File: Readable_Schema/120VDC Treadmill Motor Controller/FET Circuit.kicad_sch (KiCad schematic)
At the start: 5 parts, among them Q2 IRFB4227PBF, U2 FOD3182

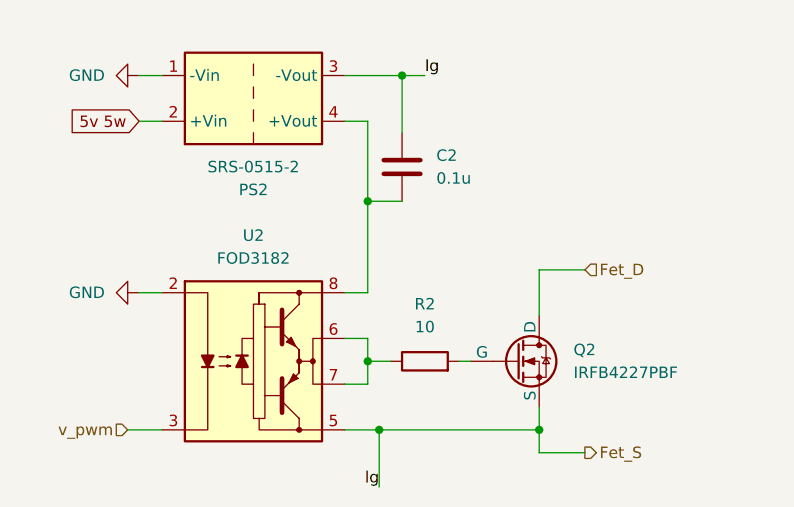
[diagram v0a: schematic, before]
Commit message: Continuing to update footprints, did some follow up math on low pass filter for adc voltage coming out of current sense system
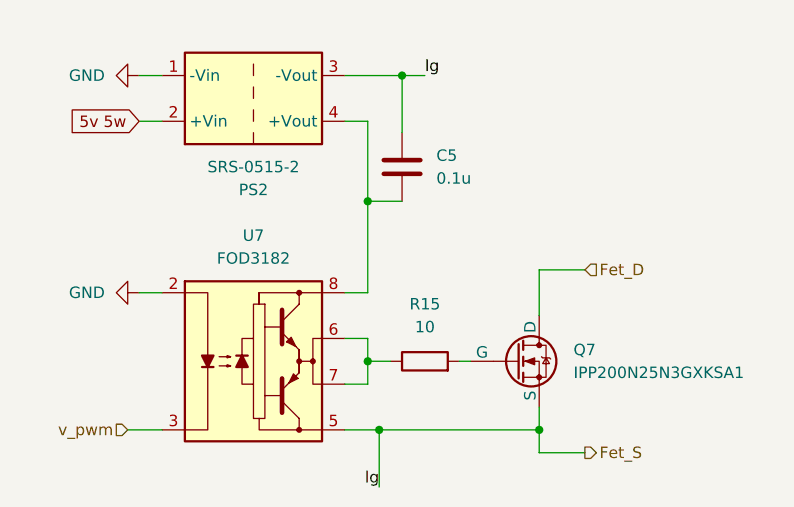
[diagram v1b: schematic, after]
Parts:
- Q7: renamed from Q2; value IRFB4227PBF -> IPP200N25N3GXKSA1
- renumbered C2 to C5, R2 to R15, U2 to U7
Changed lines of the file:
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@@
 		(dnp no)
 		(fields_autoplaced yes)
-		(property "Reference" "#PWR?"
+		(property "Reference" "#PWR0101"
 			(at 91.44 60.96 0)
 			(effects
@@
 				)
 				(path "/319bc5c0-2dd5-4df3-a34b-9170833ebccd/49a5a11b-8174-445d-b343-1fe5ec8c60de/6d3d8f4c-8a5d-4b0c-94fd-c45e8627b14b"
-					(reference "#PWR?")
+					(reference "#PWR0101")
 					(unit 1)
 				)
@@
 		(dnp no)
 		(fields_autoplaced yes)
-		(property "Reference" "#PWR?"
+		(property "Reference" "#PWR0102"
 			(at 91.44 85.09 0)
 			(effects
@@
 				)
 				(path "/319bc5c0-2dd5-4df3-a34b-9170833ebccd/49a5a11b-8174-445d-b343-1fe5ec8c60de/6d3d8f4c-8a5d-4b0c-94fd-c45e8627b14b"
-					(reference "#PWR?")
+					(reference "#PWR0102")
 					(unit 1)
 				)
@@
 		(dnp no)
 		(fields_autoplaced yes)
-		(property "Reference" "C?"
+		(property "Reference" "C5"
 			(at 130.81 69.8499 0)
 			(effects
@@
 				)
 				(path "/319bc5c0-2dd5-4df3-a34b-9170833ebccd/49a5a11b-8174-445d-b343-1fe5ec8c60de/6d3d8f4c-8a5d-4b0c-94fd-c45e8627b14b"
-					(reference "C?")
+					(reference "C5")
 					(unit 1)
 				)
@@
 		(dnp no)
 		(fields_autoplaced yes)
-		(property "Reference" "Q?"
+		(property "Reference" "Q7"
 			(at 146.05 91.4399 0)
 			(effects
@@
 			)
 		)
-		(property "Value" "IRFB4227PBF"
+		(property "Value" "IPP200N25N3GXKSA1"
 			(at 146.05 93.9799 0)
 			(effects
@@
 			)
 		)
-		(property "Datasheet" "https://www.infineon.com/assets/row/public/documents/24/49/infineon-irfb4227-datasheet-en.pdf"
+		(property "Datasheet" "https://www.infineon.com/assets/row/public/documents/24/49/infineon-ipp-b-i-200n25n3-g-datasheet-en.pdf?folderId=db3a3043163797a6011637d4bae7003b&fileId=db3a3043243b5f17012496b87e9f1971"
 			(at 139.7 105.41 0)
 			(effects
@@
 				)
 				(path "/319bc5c0-2dd5-4df3-a34b-9170833ebccd/49a5a11b-8174-445d-b343-1fe5ec8c60de/6d3d8f4c-8a5d-4b0c-94fd-c45e8627b14b"
-					(reference "Q?")
+					(reference "Q7")
 					(unit 1)
 				)
@@
 		(dnp no)
 		(fields_autoplaced yes)
-		(property "Reference" "R?"
+		(property "Reference" "R15"
 			(at 129.54 86.36 90)
 			(effects
@@
 				)
 				(path "/319bc5c0-2dd5-4df3-a34b-9170833ebccd/49a5a11b-8174-445d-b343-1fe5ec8c60de/6d3d8f4c-8a5d-4b0c-94fd-c45e8627b14b"
-					(reference "R?")
+					(reference "R15")
 					(unit 1)
 				)
@@
 		(dnp no)
 		(fields_autoplaced yes)
-		(property "Reference" "U?"
+		(property "Reference" "U7"
 			(at 110.49 78.74 0)
 			(effects
@@
 				)
 				(path "/319bc5c0-2dd5-4df3-a34b-9170833ebccd/49a5a11b-8174-445d-b343-1fe5ec8c60de/6d3d8f4c-8a5d-4b0c-94fd-c45e8627b14b"
-					(reference "U?")
-					(unit 1)
-				)
+					(reference "U7")
+					(unit 1)
+				)

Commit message: continued to add footprints, we still need to add hall effect circuit and possible brake resistor subcircuit. We may also want to consider switching the large 15v isolated power supplies to be smd as well as the FOD3182. Otherwise this will become a lot to hand solder.
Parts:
- R15: footprint (none) -> Resistor_SMD:R_0201_0603Metric_Pad0.64x0.40mm_HandSolder
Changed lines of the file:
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@@
 			)
 		)
-		(property "Footprint" ""
+		(property "Footprint" "Resistor_SMD:R_0201_0603Metric_Pad0.64x0.40mm_HandSolder"
 			(at 129.54 94.488 90)
 			(effects
@@
 			)
 		)
-		(property "Datasheet" "~"
+		(property "Datasheet" "https://industrial.panasonic.com/cdbs/www-data/pdf/RDP0000/AOA0000C337.pdf"
 			(at 129.54 92.71 0)
 			(effects
@@
 			)
 		)
-		(property "Description" "Resistor"
+		(property "Description" "ERJ-UP3J100V"
 			(at 129.54 92.71 0)
 			(effects

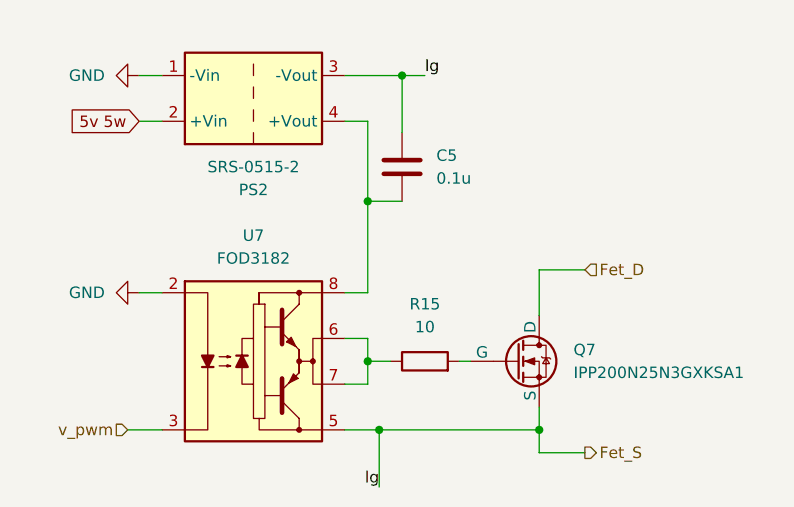
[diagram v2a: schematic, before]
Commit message: -There are no power supply/ gate driver variants for the ones chosen that support smd -We NEED to workout how we want to communicate with both linuxCNC for the CNC controller and a potentiometer for the bridgeport -We NEED to incorporate a ESTOP component that directly shuts off the motor -Missing brake resistor subcircuit -Missing Input capacitors to deal with back EMF
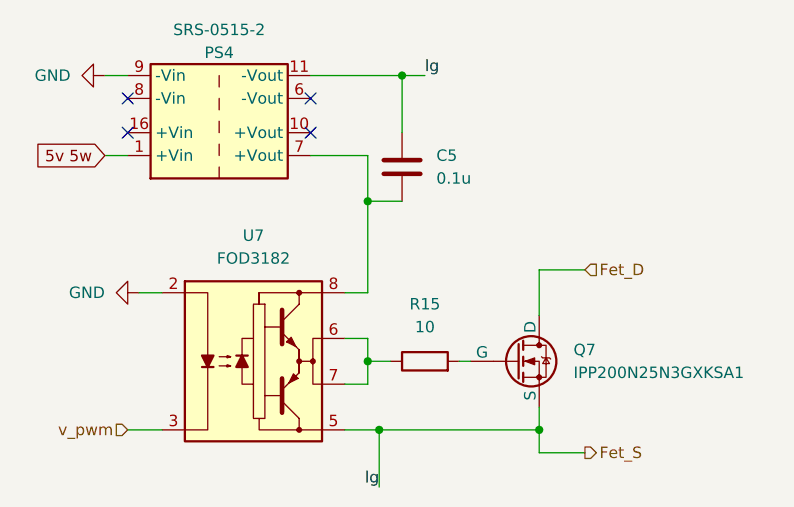
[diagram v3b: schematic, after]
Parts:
- removed PS2: SRS-0515-2, Footprints_TMC:SRS-0515 DIP-16_W7.62mm, symbol Converter_DCDC:MEE1S0303SC
- added PS4: SRS-0515-2, Footprints_TMC:SRS-0515 DIP-16_W7.62mm, symbol Treadmill_Comp:SRS-0515-2
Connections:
- net 5v 5w: now also PS4.1 (+Vin)
- net Fet_S: now also PS4.11 (-Vout)
- net GND: now also PS4.9 (-Vin)
- net at C5.2, U7.8 (VCC): now also PS4.7 (+Vout)
- no-connect marks 0 -> 4
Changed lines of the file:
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@@
 		(color 0 0 0 0)
 	)
-	(wire
-		(pts
-			(xy 97.79 60.96) (xy 100.33 60.96)
+	(no_connect
+		(at 96.52 67.31)
+	)
+	(no_connect
+		(at 116.84 63.5)
+	)
+	(no_connect
+		(at 96.52 63.5)
+	)
+	(no_connect
+		(at 116.84 67.31)
+	)
+	(wire
+		(pts
+			(xy 123.19 69.85) (xy 123.19 74.93)
 		)
 		(stroke
@@
 	(wire
 		(pts
-			(xy 120.65 60.96) (xy 127 60.96)
+			(xy 93.98 69.85) (xy 96.52 69.85)
 		)
 		(stroke
@@
 	(wire
 		(pts
-			(xy 97.79 66.04) (xy 100.33 66.04)
+			(xy 116.84 69.85) (xy 123.19 69.85)
 		)
 		(stroke
@@
 	(wire
 		(pts
+			(xy 116.84 60.96) (xy 127 60.96)
+		)
+		(stroke
+			(width 0)
+			(type default)
+		)
+	)
+	(wire
+		(pts
+			(xy 93.98 60.96) (xy 96.52 60.96)
+		)
+		(stroke
+			(width 0)
+			(type default)
+		)
+	)
+	(wire
+		(pts
 			(xy 120.65 85.09) (xy 123.19 85.09)
 		)
@@
 	(wire
 		(pts
-			(xy 120.65 66.04) (xy 123.19 66.04)
-		)
-		(stroke
-			(width 0)
-			(type default)
-		)
-	)
-	(wire
-		(pts
 			(xy 96.52 100.33) (xy 100.33 100.33)
-		)
-		(stroke
-			(width 0)
-			(type default)
-		)
-	)
-	(wire
-		(pts
-			(xy 123.19 66.04) (xy 123.19 74.93)
 		)
 		(stroke
@@
 	(global_label "5v 5w"
 		(shape input)
-		(at 97.79 66.04 180)
+		(at 93.98 69.85 180)
 		(fields_autoplaced yes)
 		(effects
@@
 		)
 		(property "Intersheetrefs" "${INTERSHEET_REFS}"
-			(at 89.1201 66.04 0)
+			(at 85.3101 69.85 0)
 			(effects
 				(font
@@
 	)
 	(symbol
-		(lib_id "power:GND")
-		(at 97.79 60.96 270)
+		(lib_id "Treadmill_Comp:SRS-0515-2")
+		(at 106.68 67.31 0)
+		(mirror x)
 		(unit 1)
 		(exclude_from_sim no)
@@
 		(on_board yes)
 		(dnp no)
-		(fields_autoplaced yes)
-		(property "Reference" "#PWR0101"
-			(at 91.44 60.96 0)
-			(effects
-				(font
-					(size 1.27 1.27)
-				)
-				(hide yes)
-			)
-		)
-		(property "Value" "GND"
-			(at 93.98 60.9599 90)
-			(effects
-				(font
-					(size 1.27 1.27)
-				)
-				(justify right)
-			)
-		)
-		(property "Footprint" ""
-			(at 97.79 60.96 0)
-			(effects
-				(font
-					(size 1.27 1.27)
-				)
-				(hide yes)
-			)
-		)
-		(property "Datasheet" ""
-			(at 97.79 60.96 0)
-			(effects
-				(font
-					(size 1.27 1.27)
-				)
-				(hide yes)
-			)
-		)
-		(property "Description" "Power symbol creates a global label with name \"GND\" , ground"
-			(at 97.79 60.96 0)
-			(effects
-				(font
-					(size 1.27 1.27)
-				)
-				(hide yes)
-			)
+		(property "Reference" "PS4"
+			(at 106.68 58.42 0)
+			(effects
+				(font
+					(size 1.27 1.27)
+				)
+			)
+		)
+		(property "Value" "SRS-0515-2"
+			(at 106.68 55.88 0)
+			(effects
+				(font
+					(size 1.27 1.27)
+				)
+			)
+		)
+		(property "Footprint" "Footprints_TMC:SRS-0515 DIP-16_W7.62mm"
+			(at 80.01 60.96 0)
+			(effects
+				(font
+					(size 1.27 1.27)
+				)
+				(justify left)
+				(hide yes)
+			)
+		)
+		(property "Datasheet" "https://www.meanwellusa.com/upload/pdf/SRS/SRS-spec.pdf"
+			(at 133.35 59.69 0)
+			(effects
+				(font
+					(size 1.27 1.27)
+				)
+				(justify left)
+				(hide yes)
+			)
+		)
+		(property "Description" "15V isolated output"
+			(at 106.68 67.31 0)
+			(effects
+				(font
+					(size 1.27 1.27)
+				)
+				(hide yes)
+			)
+		)
+		(pin "9"
 		)
 		(pin "1"
+		)
+		(pin "16"
+		)
+		(pin "8"
+		)
+		(pin "7"
+		)
+		(pin "10"
+		)
+		(pin "6"
+		)
+		(pin "11"
 		)
 		(instances
 			(project "120VDC Treadmill Motor Controller"
 				(path "/319bc5c0-2dd5-4df3-a34b-9170833ebccd/49a5a11b-8174-445d-b343-1fe5ec8c60de/0ee8c600-4f6e-4877-94f0-4a0da87ba88d"
-					(reference "#PWR05")
+					(reference "PS5")
 					(unit 1)
 				)
 				(path "/319bc5c0-2dd5-4df3-a34b-9170833ebccd/49a5a11b-8174-445d-b343-1fe5ec8c60de/6d3d8f4c-8a5d-4b0c-94fd-c45e8627b14b"
-					(reference "#PWR0101")
+					(reference "PS4")
 					(unit 1)
 				)
@@
 	)
 	(symbol
-		(lib_id "Converter_DCDC:MEE1S0303SC")
-		(at 110.49 63.5 0)
+		(lib_id "power:GND")
+		(at 93.98 60.96 270)
 		(mirror x)
 		(unit 1)
@@
 		(on_board yes)
 		(dnp no)
-		(property "Reference" "PS2"
-			(at 110.49 73.66 0)
-			(effects
-				(font
-					(size 1.27 1.27)
-				)
-			)
-		)
-		(property "Value" "SRS-0515-2"
-			(at 110.49 71.12 0)
-			(effects
-				(font
-					(size 1.27 1.27)
-				)
-			)
-		)
-		(property "Footprint" "Footprints_TMC:SRS-0515 DIP-16_W7.62mm"
-			(at 83.82 57.15 0)
-			(effects
-				(font
-					(size 1.27 1.27)
-				)
-				(justify left)
-				(hide yes)
-			)
-		)
-		(property "Datasheet" "http://diwellshop.cafe24.com/web/DATASHEET/01_subtitle/4_POWER/2_DC-DC/SRS-0515-2/SR.pdf"
-			(at 137.16 55.88 0)
-			(effects
-				(font
-					(size 1.27 1.27)
-				)
-				(justify left)
-				(hide yes)
-			)
-		)
-		(property "Description" "isolated 1W 5V to 15V DC to DC Converter"
-			(at 110.49 63.5 0)
-			(effects
-				(font
-					(size 1.27 1.27)
-				)
-				(hide yes)
-			)
-		)
-		(pin "3"
-		)
-		(pin "4"
+		(fields_autoplaced yes)
+		(property "Reference" "#PWR025"
+			(at 87.63 60.96 0)
+			(effects
+				(font
+					(size 1.27 1.27)
+				)
+				(hide yes)
+			)
+		)
+		(property "Value" "GND"
+			(at 90.17 60.9601 90)
+			(effects
+				(font
+					(size 1.27 1.27)
+				)
+				(justify right)
+			)
+		)
+		(property "Footprint" ""
+			(at 93.98 60.96 0)
+			(effects
+				(font
+					(size 1.27 1.27)
+				)
+				(hide yes)
+			)
+		)
+		(property "Datasheet" ""
+			(at 93.98 60.96 0)
+			(effects
+				(font
+					(size 1.27 1.27)
+				)
+				(hide yes)
+			)
+		)
+		(property "Description" "Power symbol creates a global label with name \"GND\" , ground"
+			(at 93.98 60.96 0)
+			(effects
+				(font
+					(size 1.27 1.27)
+				)
+				(hide yes)
+			)
 		)
 		(pin "1"
-		)
-		(pin "2"
 		)
 		(instances
 			(project "120VDC Treadmill Motor Controller"
 				(path "/319bc5c0-2dd5-4df3-a34b-9170833ebccd/49a5a11b-8174-445d-b343-1fe5ec8c60de/0ee8c600-4f6e-4877-94f0-4a0da87ba88d"
-					(reference "PS3")
+					(reference "#PWR028")
 					(unit 1)
 				)
 				(path "/319bc5c0-2dd5-4df3-a34b-9170833ebccd/49a5a11b-8174-445d-b343-1fe5ec8c60de/6d3d8f4c-8a5d-4b0c-94fd-c45e8627b14b"
-					(reference "PS2")
-					(unit 1)
-				)
+					(reference "#PWR025")
+					(unit 1)
+				)

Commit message: still working to figure out what all the supporting components are for this digital gate driver.
REASONS FOR TRYING TO SWITCH:
-Longer lasting (current opto isolator led wears out)
-Get rid of bjts and delays surrounding using those
-Even though we had mitigated turning on and off the high and low side to short at the same time, we didnt do so in a way that works with noise, this new gate driver allows for a supposedly much better handle on noise and isolates the high and low side for us
-Additionally consistency of this digital gate driver should be higher given that you are not relying on bjt resistor sizing to drive delays
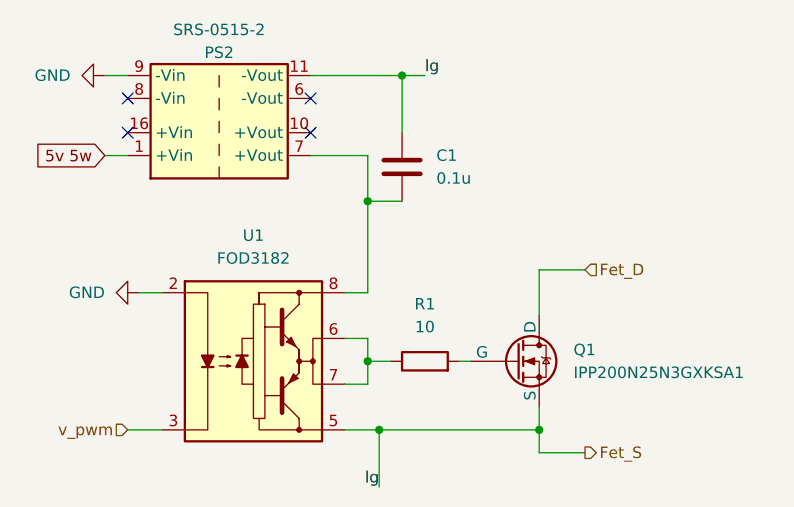
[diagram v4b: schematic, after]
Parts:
- renumbered C5 to C1, PS4 to PS2, Q7 to Q1, R15 to R1, U7 to U1
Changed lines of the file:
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@@
 		(on_board yes)
 		(dnp no)
-		(property "Reference" "PS4"
+		(property "Reference" "PS2"
 			(at 106.68 58.42 0)
 			(effects
@@
 		(instances
 			(project "120VDC Treadmill Motor Controller"
-				(path "/319bc5c0-2dd5-4df3-a34b-9170833ebccd/49a5a11b-8174-445d-b343-1fe5ec8c60de/0ee8c600-4f6e-4877-94f0-4a0da87ba88d"
-					(reference "PS5")
-					(unit 1)
-				)
-				(path "/319bc5c0-2dd5-4df3-a34b-9170833ebccd/49a5a11b-8174-445d-b343-1fe5ec8c60de/6d3d8f4c-8a5d-4b0c-94fd-c45e8627b14b"
-					(reference "PS4")
+				(path "/319bc5c0-2dd5-4df3-a34b-9170833ebccd/49a5a11b-8174-445d-b343-1fe5ec8c60de/fa17400a-1ec4-43b4-b1cb-0b7faf3eb3c2"
+					(reference "PS2")
 					(unit 1)
 				)
@@
 		(dnp no)
 		(fields_autoplaced yes)
-		(property "Reference" "#PWR0102"
+		(property "Reference" "#PWR06"
 			(at 91.44 85.09 0)
 			(effects
@@
 		(instances
 			(project "120VDC Treadmill Motor Controller"
-				(path "/319bc5c0-2dd5-4df3-a34b-9170833ebccd/49a5a11b-8174-445d-b343-1fe5ec8c60de/0ee8c600-4f6e-4877-94f0-4a0da87ba88d"
+				(path "/319bc5c0-2dd5-4df3-a34b-9170833ebccd/49a5a11b-8174-445d-b343-1fe5ec8c60de/fa17400a-1ec4-43b4-b1cb-0b7faf3eb3c2"
 					(reference "#PWR06")
-					(unit 1)
-				)
-				(path "/319bc5c0-2dd5-4df3-a34b-9170833ebccd/49a5a11b-8174-445d-b343-1fe5ec8c60de/6d3d8f4c-8a5d-4b0c-94fd-c45e8627b14b"
-					(reference "#PWR0102")
 					(unit 1)
 				)
@@
 		(dnp no)
 		(fields_autoplaced yes)
-		(property "Reference" "C5"
+		(property "Reference" "C1"
 			(at 130.81 69.8499 0)
 			(effects
@@
 		(instances
 			(project "120VDC Treadmill Motor Controller"
-				(path "/319bc5c0-2dd5-4df3-a34b-9170833ebccd/49a5a11b-8174-445d-b343-1fe5ec8c60de/0ee8c600-4f6e-4877-94f0-4a0da87ba88d"
-					(reference "C2")
-					(unit 1)
-				)
-				(path "/319bc5c0-2dd5-4df3-a34b-9170833ebccd/49a5a11b-8174-445d-b343-1fe5ec8c60de/6d3d8f4c-8a5d-4b0c-94fd-c45e8627b14b"
-					(reference "C5")
+				(path "/319bc5c0-2dd5-4df3-a34b-9170833ebccd/49a5a11b-8174-445d-b343-1fe5ec8c60de/fa17400a-1ec4-43b4-b1cb-0b7faf3eb3c2"
+					(reference "C1")
 					(unit 1)
 				)
@@
 		(dnp no)
 		(fields_autoplaced yes)
-		(property "Reference" "Q7"
+		(property "Reference" "Q1"
 			(at 146.05 91.4399 0)
 			(effects
@@
 		(instances
 			(project "120VDC Treadmill Motor Controller"
-				(path "/319bc5c0-2dd5-4df3-a34b-9170833ebccd/49a5a11b-8174-445d-b343-1fe5ec8c60de/0ee8c600-4f6e-4877-94f0-4a0da87ba88d"
-					(reference "Q2")
-					(unit 1)
-				)
-				(path "/319bc5c0-2dd5-4df3-a34b-9170833ebccd/49a5a11b-8174-445d-b343-1fe5ec8c60de/6d3d8f4c-8a5d-4b0c-94fd-c45e8627b14b"
-					(reference "Q7")
+				(path "/319bc5c0-2dd5-4df3-a34b-9170833ebccd/49a5a11b-8174-445d-b343-1fe5ec8c60de/fa17400a-1ec4-43b4-b1cb-0b7faf3eb3c2"
+					(reference "Q1")
 					(unit 1)
 				)
@@
 		(dnp no)
 		(fields_autoplaced yes)
-		(property "Reference" "#PWR025"
+		(property "Reference" "#PWR04"
 			(at 87.63 60.96 0)
 			(effects
@@
 		(instances
 			(project "120VDC Treadmill Motor Controller"
-				(path "/319bc5c0-2dd5-4df3-a34b-9170833ebccd/49a5a11b-8174-445d-b343-1fe5ec8c60de/0ee8c600-4f6e-4877-94f0-4a0da87ba88d"
-					(reference "#PWR028")
-					(unit 1)
-				)
-				(path "/319bc5c0-2dd5-4df3-a34b-9170833ebccd/49a5a11b-8174-445d-b343-1fe5ec8c60de/6d3d8f4c-8a5d-4b0c-94fd-c45e8627b14b"
-					(reference "#PWR025")
+				(path "/319bc5c0-2dd5-4df3-a34b-9170833ebccd/49a5a11b-8174-445d-b343-1fe5ec8c60de/fa17400a-1ec4-43b4-b1cb-0b7faf3eb3c2"
+					(reference "#PWR04")
 					(unit 1)
 				)
@@
 		(dnp no)
 		(fields_autoplaced yes)
-		(property "Reference" "R15"
+		(property "Reference" "R1"
 			(at 129.54 86.36 90)
 			(effects
@@
 		(instances
 			(project "120VDC Treadmill Motor Controller"
-				(path "/319bc5c0-2dd5-4df3-a34b-9170833ebccd/49a5a11b-8174-445d-b343-1fe5ec8c60de/0ee8c600-4f6e-4877-94f0-4a0da87ba88d"
-					(reference "R2")
-					(unit 1)
-				)
-				(path "/319bc5c0-2dd5-4df3-a34b-9170833ebccd/49a5a11b-8174-445d-b343-1fe5ec8c60de/6d3d8f4c-8a5d-4b0c-94fd-c45e8627b14b"
-					(reference "R15")
+				(path "/319bc5c0-2dd5-4df3-a34b-9170833ebccd/49a5a11b-8174-445d-b343-1fe5ec8c60de/fa17400a-1ec4-43b4-b1cb-0b7faf3eb3c2"
+					(reference "R1")
 					(unit 1)
 				)
@@
 		(dnp no)
 		(fields_autoplaced yes)
-		(property "Reference" "U7"
+		(property "Reference" "U1"
 			(at 110.49 78.74 0)
 			(effects
@@
 		(instances
 			(project "120VDC Treadmill Motor Controller"
-				(path "/319bc5c0-2dd5-4df3-a34b-9170833ebccd/49a5a11b-8174-445d-b343-1fe5ec8c60de/0ee8c600-4f6e-4877-94f0-4a0da87ba88d"
-					(reference "U2")
-					(unit 1)
-				)
-				(path "/319bc5c0-2dd5-4df3-a34b-9170833ebccd/49a5a11b-8174-445d-b343-1fe5ec8c60de/6d3d8f4c-8a5d-4b0c-94fd-c45e8627b14b"
-					(reference "U7")
-					(unit 1)
-				)
+				(path "/319bc5c0-2dd5-4df3-a34b-9170833ebccd/49a5a11b-8174-445d-b343-1fe5ec8c60de/fa17400a-1ec4-43b4-b1cb-0b7faf3eb3c2"
+					(reference "U1")
+					(unit 1)
+				)
